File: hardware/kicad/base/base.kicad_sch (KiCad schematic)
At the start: 21 parts, among them J1 TYPE-C-31-M-12, J2 BATT, J3 LINK, Q1 BSS138DW, SW1 TS-1187A, U1 BQ25180YBGR, U2 USBLC6-2SC6

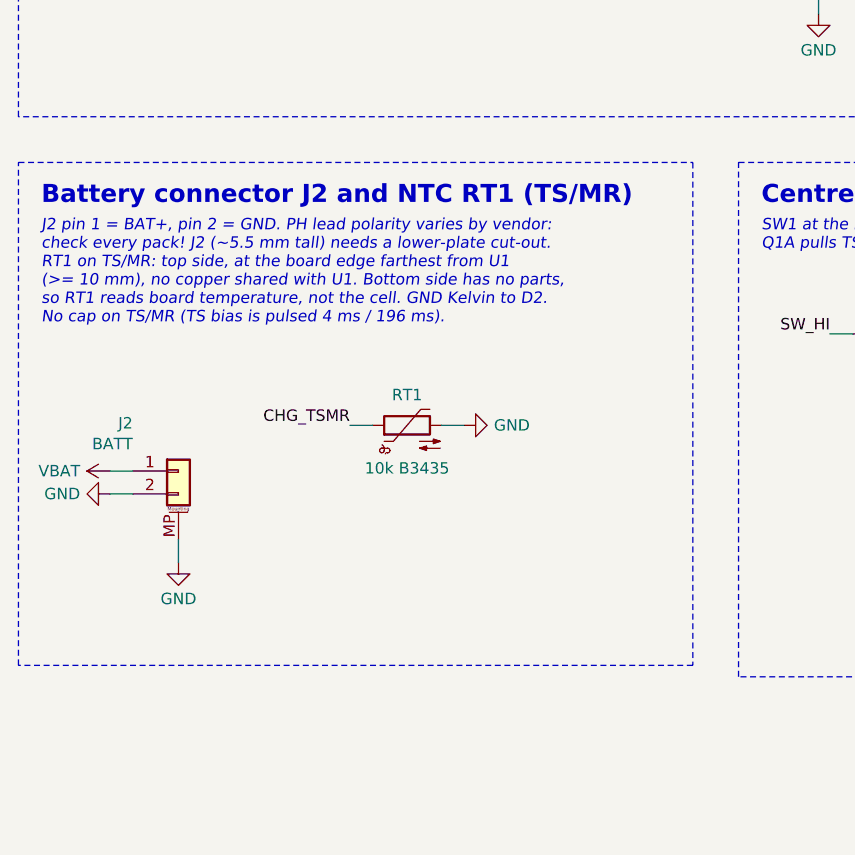
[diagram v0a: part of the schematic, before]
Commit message: Mechanical fit: SH battery connector, module u.FL outward, J1 out of the hub zone
- base J2: JST SH 4-pin side-entry (PH was too tall under the pressed rotor web)
- main: MDBT50Q inner end r >= 8.8 with u.FL facing out; J1 at r 19.5; top r <= 4.6
  kept for the spindle nut; low-profile-only actuator corridor on the bottom
- placer: keep-outs can exempt footprints (low-profile parts)
- enclosure model: coax and battery-lead paths follow the new placement; clash check
  shows only the intended contacts
- docs synced to the earlier late-change list; SPEC updated

Co-Authored-By: Claude Opus 5.5 <noreply@anthropic.com>
Claude-Session: https://claude.ai/code/session_01P3cqdBhxLcWY3sGUVf9LAJ
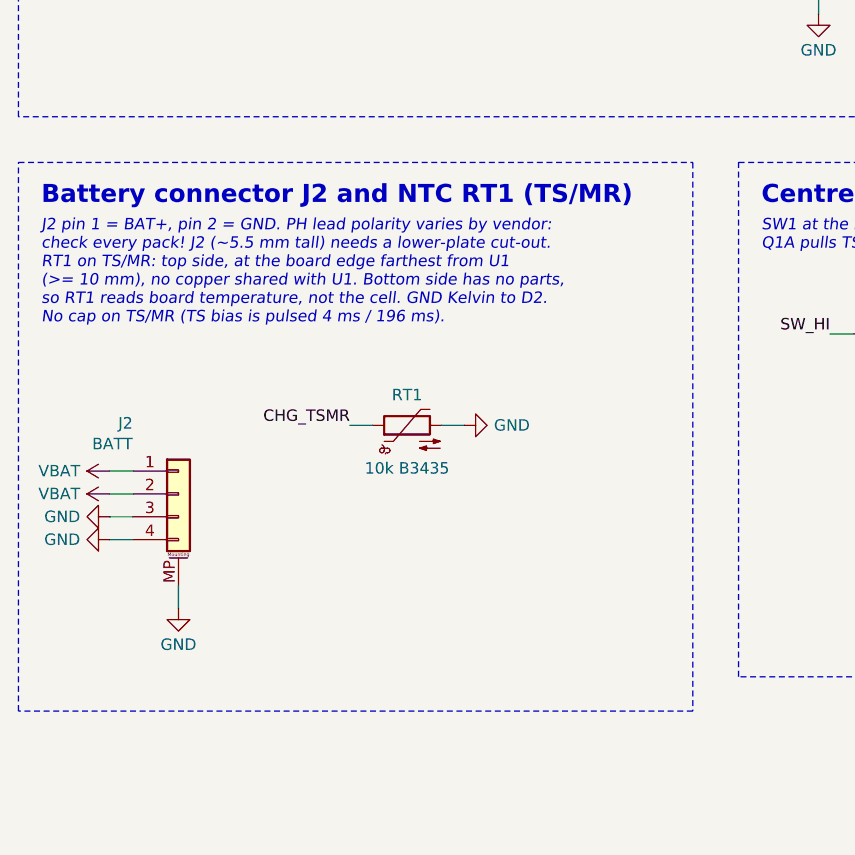
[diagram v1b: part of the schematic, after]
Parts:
- J2: footprint Connector_JST:JST_PH_S2B-PH-SM4-TB_1x02-1MP_P2.00mm_Horizontal -> Connector_JST:JST_SH_SM04B-SRSS-TB_1x04-1MP_P1.00mm_Horizontal; symbol Connector_Generic_MountingPin:Conn_01x02_MountingPin -> Connector_Generic_MountingPin:Conn_01x04_MountingPin; LCSC C295747 -> C160404; MPN S2B-PH-SM4-TB(LF)(SN) -> SM04B-SRSS-TB(LF)(SN)
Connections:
- net GND: now also J2.3 (Pin_3), J2.4 (Pin_4); no longer J2.2 (Pin_2)
- net VBAT: now also J2.2 (Pin_2)

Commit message: SPICE findings (sources): U21 QOD to OLED_VIN, R4 68R, R12 4R7, 25 V VSYS caps, base R4 100k, C1 0805 X7R
Netlists are regenerated once the last two SPICE verifications finish.

Co-Authored-By: Claude Opus 5.5 <noreply@anthropic.com>
Claude-Session: https://claude.ai/code/session_01P3cqdBhxLcWY3sGUVf9LAJ
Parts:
- C1: footprint Capacitor_SMD:C_0603_1608Metric -> Capacitor_SMD:C_0805_2012Metric; LCSC C309478 -> C277470; MPN CC0603KRX5R8BB225 -> CC0805KKX7R8BB225
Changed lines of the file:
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@@
 			)
 		)
-		(property "Footprint" "Capacitor_SMD:C_0603_1608Metric"
+		(property "Footprint" "Capacitor_SMD:C_0805_2012Metric"
 			(at 264.16 38.1 0)
 			(effects
@@
 			)
 		)
-		(property "MPN" "CC0603KRX5R8BB225"
+		(property "MPN" "CC0805KKX7R8BB225"
 			(at 264.16 38.1 0)
 			(effects
@@
 			)
 		)
-		(property "LCSC" "C309478"
+		(property "LCSC" "C277470"
 			(at 264.16 38.1 0)
 			(effects

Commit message: Base board goes 4-layer (In1 GND plane); fix In1 power-plane marking for KiCad 9 (layer id 4)
The 2-layer base never routed completely (J3 signals and the button/charger network had to
cross the power tracks with GND routed as tracks). set_layer_types matched '(1 "In1.Cu" ...)',
but KiCad 9 numbers In1 as layer 4, so the main board's GND plane was routed as a signal layer too.

Co-Authored-By: Claude Opus 5.5 <noreply@anthropic.com>
Claude-Session: https://claude.ai/code/session_01P3cqdBhxLcWY3sGUVf9LAJ
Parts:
- C4: value 10u -> 10u/25V; LCSC C19702 -> C96446; MPN CL10A106KP8NNNC -> CL10A106MA8NRNC
- R4: value 1M -> 100k; LCSC C26083 -> C25741; MPN 0402WGF1004TCE -> 0402WGF1003TCE
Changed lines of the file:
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@@
 			)
 		)
-		(property "Value" "1M"
+		(property "Value" "100k"
 			(at 154.94 124.536 90)
 			(effects
@@
 			)
 		)
-		(property "MPN" "0402WGF1004TCE"
+		(property "MPN" "0402WGF1003TCE"
 			(at 154.94 121.92 0)
 			(effects
@@
 			)
 		)
-		(property "LCSC" "C26083"
+		(property "LCSC" "C25741"
 			(at 154.94 121.92 0)
 			(effects
@@
 			)
 		)
-		(property "Value" "10u"
+		(property "Value" "10u/25V"
 			(at 271.78 128.092 90)
 			(effects
@@
 			)
 		)
-		(property "MPN" "CL10A106KP8NNNC"
+		(property "MPN" "CL10A106MA8NRNC"
 			(at 271.78 124.46 0)
 			(effects
@@
 			)
 		)
-		(property "LCSC" "C19702"
+		(property "LCSC" "C96446"
 			(at 271.78 124.46 0)
 			(effects

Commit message: Schematic notes: J1 at r 19.5, VLED fall 24/26.6 ms, hot-plug 4.49-5.49 V, SM04B J2, 100k press pull-down, SYS_REG 4.4 V, side-entry J3, LED data path and margins
Notes only; netlists unchanged. Base board still DRC-clean with schematic parity.

Co-Authored-By: Claude Opus 5.5 <noreply@anthropic.com>
Claude-Session: https://claude.ai/code/session_01P3cqdBhxLcWY3sGUVf9LAJ
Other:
- note added: "IN 2.2u/25V, SYS 10u/25V, BAT 4.7u: each within 1 mm of its ball and of the D2 GND ball. SYS = VSYS (4.4 V on USB, SYS_REG set by firmware; VBAT on battery). /INT, SCL, SDA pull-ups are on the main board."
- note added: "J2 SM04B side-entry SH (2.95 mm): pins 1-2 = BAT+, 3-4 = GND (two 28 AWG leads per rail). Packs are re-terminated: check the polarity of every pack. RT1 on TS/MR: top side, at the board edge farthest from U1 (>= 10 mm), no copper shared with U1. Bottom side has no parts, so RT1 reads board temperature, not the cell. GND Kelvin to D2. No cap on TS/MR (TS bias is pulsed 4 ms / 196 ms)."
- note added: "JST SH 12-way SIDE-entry (SM12B, 2.95 mm) at r 15.5, θ 120°, entry facing the centre; identical pinout on the main board (SPEC §2). C4 sits next to J3. The harness runs into the spindle's side slot."
- note added: "SW1 at the board centre (top). Press: VBAT -> 1k -> SW1 -> SW_GATE (100k to GND, ~42 uA while held; the gates discharge within the BQ25180 deglitch on release). Q1A pulls TS/MR low (ship wake / 20 s HW reset); Q1B pulls BTN_N low (nRF SENSE wake). BTN_N pull-up is on main."
- note removed: "IN 2.2u/25V, SYS 10u/25V, BAT 4.7u: each within 1 mm of its ball and of the D2 GND ball. SYS = VSYS (4.5 V on USB, VBAT on battery). /INT, SCL, SDA pull-ups are on the main board."
- note removed: "J2 pin 1 = BAT+, pin 2 = GND. PH lead polarity varies by vendor: check every pack! J2 (~5.5 mm tall) needs a lower-plate cut-out. RT1 on TS/MR: top side, at the board edge farthest from U1 (>= 10 mm), no copper shared with U1. Bottom side has no parts, so RT1 reads board temperature, not the cell. GND Kelvin to D2. No cap on TS/MR (TS bias is pulsed 4 ms / 196 ms)."
- note removed: "JST SH 12-way vertical; identical pinout on the main board (SPEC §2). C4 sits next to J3. Only 1.7 mm (~1.2 mm pressed) under the FA lower plate: J3 + mated SHR plug need a plate cut-out (the harness exits through it into the spindle)."
- note removed: "SW1 at the board centre (top). Press: VBAT -> 1k -> SW1 -> SW_GATE (1M to GND, ~4 uA while held). Q1A pulls TS/MR low (ship wake / 20 s HW reset); Q1B pulls BTN_N low (nRF SENSE wake). BTN_N pull-up is on main."
- moved on the sheet: C4, J3, Q1A, Q1B, R3, R4, SW1, TP1, TP2, TP3, TP4
